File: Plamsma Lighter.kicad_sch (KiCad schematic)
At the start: 5 parts, among them Q1 NPN, SW2 SW_Push

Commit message: Updated schematic.
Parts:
- removed SW2: SW_Push, symbol Switch:SW_Push
- added C1: C, symbol Device:C
- TR1: value TRANSF3 -> 16:1000
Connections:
- net GND: now also C1.2
- net at D1.1 (K): now also Q1.2 (B)
- net at Q1.1 (C): now also TR1.3, C1.1
- net at TR1.5: now also R1.1; no longer Q1.2 (B)
- net VCC renamed 3.7V
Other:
- note added: "1000T"
- note added: "8T"
- moved on the sheet: D1, Q1, R1

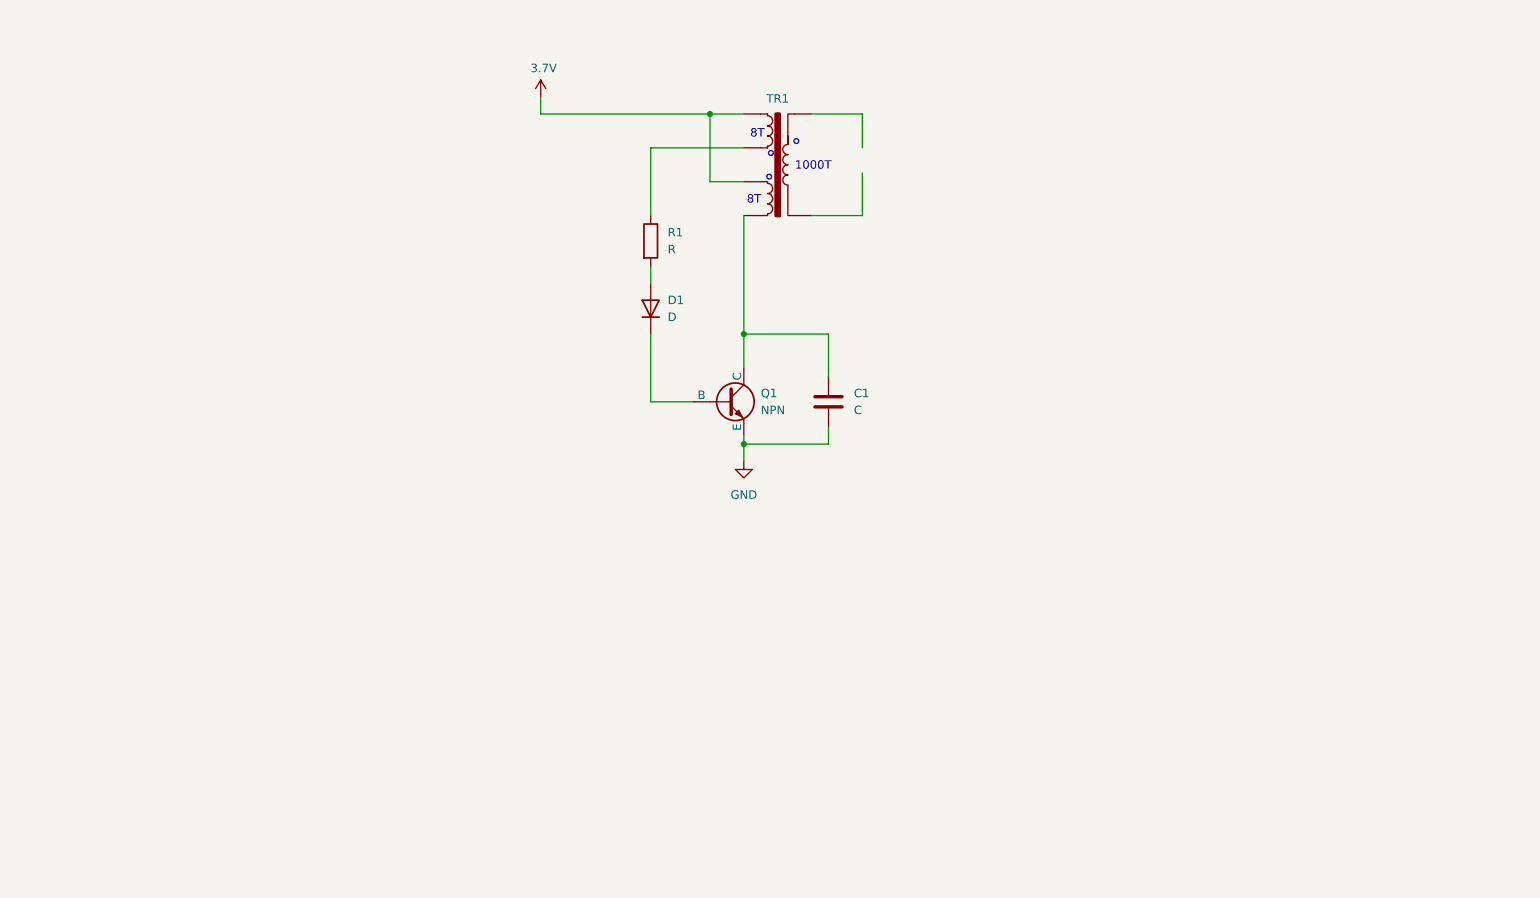
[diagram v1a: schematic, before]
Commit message: Finished prototype Schematic.
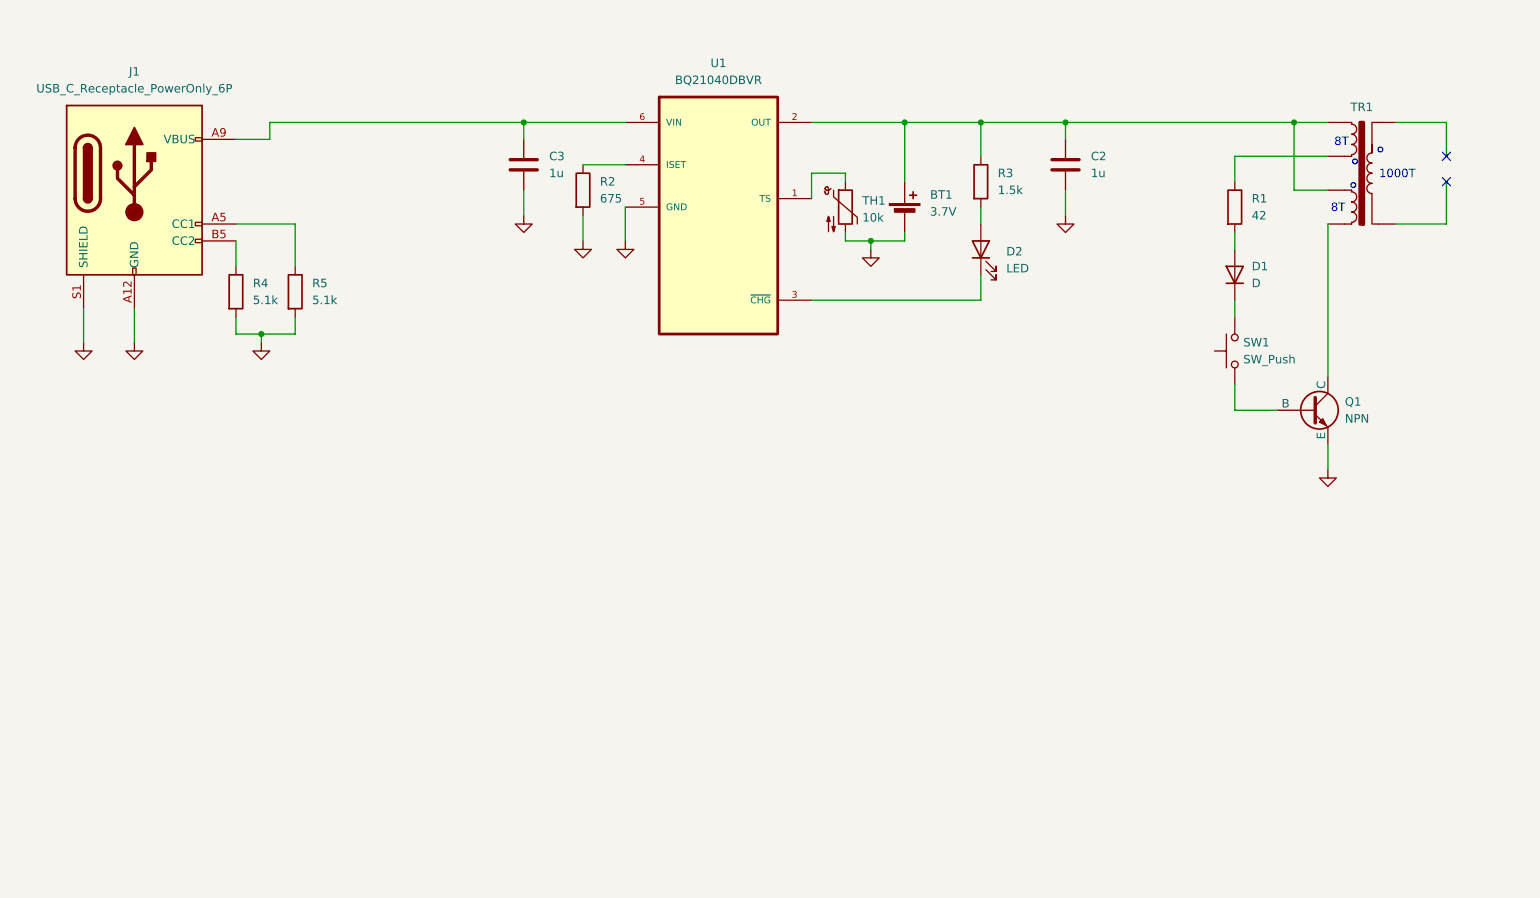
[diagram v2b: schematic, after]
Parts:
- removed C1: C, symbol Device:C
- added BT1: 3.7V, symbol Device:Battery_Cell
- added C2, C3: 1u, symbol Device:C
- added D2: LED, symbol Device:LED
- added J1: USB_C_Receptacle_PowerOnly_6P, symbol Connector:USB_C_Receptacle_PowerOnly_6P
- added R2: 675, symbol Device:R
- added R3: 1.5k, symbol Device:R
- added R4, R5: 5.1k, symbol Device:R
- added SW1: SW_Push, symbol Switch:SW_Push
- added TH1: 10k, symbol Device:Thermistor_NTC
- added U1: BQ21040DBVR, BQ21040DBVR:SOT95P280X145-6N, symbol AlphaF:BQ21040DBVR
- R1: value R -> 42
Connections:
- net GND: now also BT1.2 (-), C2.2, C3.2, J1.A12 (GND), J1.B12 (GND), J1.S1 (SHIELD), R2.2, R4.2, R5.2, TH1.2, U1.5 (GND)
- net at Q1.2 (B): now also SW1.1; no longer D1.1 (K)
- net 3.7V: no longer names the net of TR1.4, TR1.6
- net 3.7V: now also BT1.1 (+), C2.1, R3.1, U1.2 (OUT)
- new net: D2.1 (K), U1.3 (~{CHG})
- new net: D2.2 (A), R3.2
- new net: J1.B5 (CC2), R4.1
- new net: J1.A5 (CC1), R5.1
- new net: D1.1 (K), SW1.2
- new net: TH1.1, U1.1 (TS)
- new net: R2.1, U1.4 (ISET)
- new net: C3.1, J1.A9 (VBUS), J1.B9 (VBUS), U1.6 (VIN)
- no-connect marks 0 -> 2
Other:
- moved on the sheet: D1, Q1, R1, TR1

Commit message: Added lion battery level indicator to schematic.
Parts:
- added D3, D4, D5, D6, D8: LED, symbol Device:LED
- added D7: D, symbol Device:D
- added R10, R11, R12, R13, R14, R15, R16, R17, R6, R7, R8, R9: R, symbol Device:R
- added U2: LM339DR, AlphaF:SOIC127P600X175-14N, symbol AlphaF:LM339DR
- BT1: value 3.7V -> 3-4.2V
- C1: renamed from C3; footprint (none) -> Capacitor_SMD:C_0603_1608Metric_Pad1.08x0.95mm_HandSolder
- C2: footprint (none) -> Capacitor_SMD:C_0603_1608Metric_Pad1.08x0.95mm_HandSolder
- D1: renamed from D2; footprint (none) -> Diode_SMD:D_0603_1608Metric_Pad1.05x0.95mm_HandSolder
- J1: footprint (none) -> AlphaF:GCT_USB4125-GF-A_REVA2
- R1: renamed from R4; footprint (none) -> Resistor_SMD:R_0603_1608Metric_Pad0.98x0.95mm_HandSolder
- R2: renamed from R5; footprint (none) -> Resistor_SMD:R_0603_1608Metric_Pad0.98x0.95mm_HandSolder
- R3: renamed from R2; footprint (none) -> Resistor_SMD:R_0603_1608Metric_Pad0.98x0.95mm_HandSolder
- R4: renamed from R3; footprint (none) -> Resistor_SMD:R_0603_1608Metric_Pad0.98x0.95mm_HandSolder
- U1: footprint BQ21040DBVR:SOT95P280X145-6N -> AlphaF:SOT95P280X145-6N
- renumbered D1 to D2, R1 to R5
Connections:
- net GND: now also D7.1 (K), D8.1 (K), R11.2, R17.2
- new net: R9.1, U2.13 (OUT4)
- new net: D6.1 (K), R9.2
- new net: D8.2 (A), R12.2, R13.1
- new net: R13.2, R14.1, U2.7 (1IN+)
- new net: R6.1, U2.1 (1OUT)
- new net: D3.1 (K), R6.2
- new net: D4.1 (K), R7.2
- new net: R7.1, U2.2 (2OUT)
- new net: R8.1, U2.14 (OUT3)
- new net: D5.1 (K), R8.2
- new net: R14.2, R15.1, U2.5 (2IN+)
- new net: R15.2, R16.1, U2.9 (3IN+)
- new net: R10.2, R11.1, U2.10 (4IN-), U2.4 (2IN-), U2.6 (1IN-), U2.8 (3IN-)
- new net: R16.2, R17.1, U2.11 (4IN+)
- new net: D7.2 (A), U2.12 (GND)
- new net 3V-4.2V: D3.2 (A), D4.2 (A), D5.2 (A), D6.2 (A), R10.1, R12.1, U2.3 (VCC)
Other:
- moved on the sheet: BT1, C1, C2, D1, D2, J1, Q1, R1, R2, R3, R4, R5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
